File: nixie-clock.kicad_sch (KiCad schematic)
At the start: 80 parts, among them J1 I2C, J2 SWD, J3 ESP-Connector, J4 Power Input, J5 ARGB, Q1 FDS2734, SW1 PTS815, U1 TPS62175DQC, U2 STM32F103CBTx, U3 TC1185, U4 LT3757AEMSE, U5 Dot1, U6 Dot2, U7 USBLC6-2SC6

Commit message: Add PCB and update Schematic
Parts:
- removed C18: 100n, symbol Device:C
- removed D2, D3, D4, D5, D6, D7: APA102, LED_SMD:LED_RGB_5050-6, symbol LED:APA102
- removed R10, R9: 3k9, symbol Device:R
- added C21: 220n 35V, Capacitor_SMD:C_0805_2012Metric_Pad1.18x1.45mm_HandSolder, symbol Device:C
- added H7, H8, H9: MountingHole_Pad, MountingHole:MountingHole_3.2mm_M3_ISO14580, symbol Mechanical:MountingHole
- added TP1: GND, TestPoint:TestPoint_THTPad_D1.5mm_Drill0.7mm, symbol Connector:TestPoint
- added TP2: 3V3, TestPoint:TestPoint_THTPad_D1.5mm_Drill0.7mm, symbol Connector:TestPoint
- added TP3: 5V, TestPoint:TestPoint_THTPad_D1.5mm_Drill0.7mm, symbol Connector:TestPoint
- added TP4: 190V, TestPoint:TestPoint_THTPad_D1.5mm_Drill0.7mm, symbol Connector:TestPoint
- added TP5: TimeSync, TestPoint:TestPoint_THTPad_D1.5mm_Drill0.7mm, symbol Connector:TestPoint
- C1, C3: footprint (none) -> Capacitor_SMD:C_0805_2012Metric_Pad1.18x1.45mm_HandSolder
- C10: renamed from C9; footprint (none) -> Capacitor_SMD:C_0603_1608Metric_Pad1.08x0.95mm_HandSolder
- C11: renamed from C12; footprint (none) -> Capacitor_SMD:C_0603_1608Metric_Pad1.08x0.95mm_HandSolder
- C12: renamed from C11; footprint (none) -> Capacitor_SMD:C_0402_1005Metric_Pad0.74x0.62mm_HandSolder
- C13: renamed from C14; footprint (none) -> Capacitor_SMD:C_0603_1608Metric_Pad1.08x0.95mm_HandSolder
- C14: renamed from C15; footprint (none) -> Capacitor_SMD:C_0805_2012Metric_Pad1.18x1.45mm_HandSolder
- C15: renamed from C10; footprint (none) -> Capacitor_SMD:C_0603_1608Metric_Pad1.08x0.95mm_HandSolder
- C16, C20: footprint (none) -> Capacitor_SMD:C_0603_1608Metric_Pad1.08x0.95mm_HandSolder
- C17: renamed from C13; footprint (none) -> Capacitor_SMD:C_0603_1608Metric_Pad1.08x0.95mm_HandSolder
- C18: renamed from C19; footprint (none) -> Capacitor_SMD:C_0402_1005Metric_Pad0.74x0.62mm_HandSolder
- C19: renamed from C17; footprint (none) -> Capacitor_SMD:C_1206_3216Metric_Pad1.33x1.80mm_HandSolder
- C22: renamed from C21; value 10u -> 10u 16V; footprint (none) -> Capacitor_SMD:C_0805_2012Metric_Pad1.18x1.45mm_HandSolder
- C23: renamed from C22; footprint (none) -> Capacitor_SMD:C_0603_1608Metric_Pad1.08x0.95mm_HandSolder
- C4: renamed from C24; footprint (none) -> Capacitor_SMD:C_0603_1608Metric_Pad1.08x0.95mm_HandSolder
- C6: renamed from C5; footprint Capacitor_SMD:C_0603_1608Metric_Pad1.08x0.95mm_HandSolder -> Capacitor_SMD:C_0805_2012Metric_Pad1.18x1.45mm_HandSolder
- C7: renamed from C6; footprint (none) -> Capacitor_SMD:C_0805_2012Metric_Pad1.18x1.45mm_HandSolder
- C8: renamed from C7; footprint (none) -> Capacitor_SMD:C_0805_2012Metric_Pad1.18x1.45mm_HandSolder
- C9: renamed from C8; footprint (none) -> Capacitor_SMD:C_0603_1608Metric_Pad1.08x0.95mm_HandSolder
- D1: value D -> HS1FFL; footprint (none) -> Diode_SMD:D_SOD-123F
- L2: value 470u -> 470u (NS12555T471MN); footprint (none) -> extraFootprints:Taiyo Yuden NS 12.5mmx12.5mm
- R1: renamed from R60; footprint (none) -> Resistor_SMD:R_0603_1608Metric_Pad0.98x0.95mm_HandSolder
- R10: renamed from R4; footprint (none) -> Resistor_SMD:R_0603_1608Metric_Pad0.98x0.95mm_HandSolder
- R11: renamed from R5; footprint (none) -> Resistor_SMD:R_0603_1608Metric_Pad0.98x0.95mm_HandSolder
- R12: renamed from R6; footprint (none) -> Resistor_SMD:R_0603_1608Metric_Pad0.98x0.95mm_HandSolder
- R13: renamed from R7; footprint (none) -> Resistor_SMD:R_1206_3216Metric_Pad1.30x1.75mm_HandSolder
- R14: renamed from R8; footprint (none) -> Resistor_SMD:R_0603_1608Metric_Pad0.98x0.95mm_HandSolder
- R15: renamed from R65; value R -> 56k; footprint (none) -> Resistor_SMD:R_0603_1608Metric_Pad0.98x0.95mm_HandSolder
- R16: renamed from R66; value R -> 56k; footprint (none) -> Resistor_SMD:R_0603_1608Metric_Pad0.98x0.95mm_HandSolder
- R2: renamed from R59; footprint (none) -> Resistor_SMD:R_0603_1608Metric_Pad0.98x0.95mm_HandSolder
- R3: renamed from R67; footprint (none) -> Resistor_SMD:R_0603_1608Metric_Pad0.98x0.95mm_HandSolder
- R4: renamed from R1; footprint Resistor_SMD:R_0603_1608Metric_Pad1.05x0.95mm_HandSolder -> Resistor_SMD:R_0603_1608Metric_Pad0.98x0.95mm_HandSolder
- R5: renamed from R2; footprint Resistor_SMD:R_0603_1608Metric_Pad1.05x0.95mm_HandSolder -> Resistor_SMD:R_0603_1608Metric_Pad0.98x0.95mm_HandSolder
- R6: renamed from R69; footprint (none) -> Resistor_SMD:R_1206_3216Metric_Pad1.30x1.75mm_HandSolder
- R7: renamed from R70; footprint (none) -> Resistor_SMD:R_0603_1608Metric_Pad0.98x0.95mm_HandSolder
- R8: renamed from R68; footprint (none) -> Resistor_SMD:R_0603_1608Metric_Pad0.98x0.95mm_HandSolder
- R9: renamed from R3; footprint (none) -> Resistor_SMD:R_0603_1608Metric_Pad0.98x0.95mm_HandSolder
- renumbered C23 to C24, C4 to C5, D8 to D2, J4 to J1, J5 to J2, J1 to J3, J2 to J4, J3 to J5, U7 to U2, U2 to U3, U3 to U4, U4 to U5, U5 to U6, U6 to U7
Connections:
- net +24V: now also C21.1
- net +3V3: now also TP2.1
- net +5V: now also TP3.1
- net GND: now also J1.1 (Pin_1), R15.2, R16.2, C21.2, TP1.1; no longer J1.2 (Pin_2), U6.7 (K), U7.7 (K)
- net TimeSync: now also TP5.1
- net Vdrive: now also TP4.1
- net high-side-switch6/Dot: now also U6.1 (A), U7.1 (A); no longer R15.1, R16.1
- net ledClock: now also U2.1 (I/O1); no longer U2.6 (I/O1)
- net ledData: now also U2.6 (I/O1); no longer U2.4 (I/O2)
- net at J2.3 (Pin_3): now also U2.3 (I/O2)
- net at J2.2 (Pin_2): now also U2.4 (I/O2)
- net at F1.1: now also J1.2 (Pin_2); no longer J1.1 (Pin_1)
- new net: R15.1, U6.2 (K)
- new net: R16.1, U7.2 (K)
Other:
- sheet low-side-switch10 renamed low-side-switch-dp-left
- removed sheet low-side-switch11
- added sheet low-side-switch-dp-right (low-side-switch-dp.kicad_sch)
- sheet low-side-switch-dp-left: file low-side-switch.kicad_sch -> low-side-switch-dp.kicad_sch
- note added: "LED mounting"
- note added: "PCB mounting"
- note added: "Reduce Hot Loop Area to minimize EMI: Linear Technology AN139-1 Texas Instruments SNVA803"
- note added: "connector for addressable LEDs"
- note added: "test points"
- note removed: "addressable LEDs"
- note removed: "mounting"
- moved on the sheet: C15, C16, C17, C18, C19, C20, C22, C23, C24, C4, D1, D2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

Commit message: Add dimming option
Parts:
- added C25: 100n, Capacitor_SMD:C_0603_1608Metric_Pad1.08x0.95mm_HandSolder, symbol Device:C
- added C26: 1u, Capacitor_SMD:C_0805_2012Metric_Pad1.18x1.45mm_HandSolder, symbol Device:C
- added R71: 10k, Resistor_SMD:R_0603_1608Metric_Pad0.98x0.95mm_HandSolder, symbol Device:R
- added U8: SN74HCS541, extraFootprints:VSSOP-20_5.1x3mm_P0.5mm, symbol extraSymbols:SN74HCS541
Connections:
- net +3V3: now also C25.2, C26.2, R71.1, U8.20 (V_{CC})
- net Enable.Dots: now also U8.8 (A7)
- net Enable.Tube0: now also U8.2 (A1)
- net Enable.Tube1: now also U8.3 (A2)
- net Enable.Tube2: now also U8.4 (A3)
- net Enable.Tube3: now also U8.5 (A4)
- net Enable.Tube4: now also U8.6 (A5)
- net Enable.Tube5: now also U8.7 (A6)
- net GND: now also C25.1, C26.1, U8.10 (GND), U8.9 (A8)
- net ~{PWM}: now reaches U3.19 (PB1)
- net ~{PWM}: now also R71.2, U8.1 (~{OE1}), U8.19 (~{OE2})
- new net high-side-switch/Enable: U8.18 (Y1)
- new net high-side-switch1/Enable: U8.17 (Y2)
- new net high-side-switch2/Enable: U8.16 (Y3)
- new net high-side-switch3/Enable: U8.15 (Y4)
- new net high-side-switch4/Enable: U8.14 (Y5)
- new net high-side-switch5/Enable: U8.13 (Y6)
- new net high-side-switch6/Enable: U8.12 (Y7)
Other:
- note added: "IC buffer for PWM dimming"
- moved on the sheet: C1, C10, C11, C12, C13, C14, C15, C16, C17, C18, C19, C2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

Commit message: Some finish workings
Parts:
- C23: footprint Capacitor_SMD:C_0603_1608Metric_Pad1.08x0.95mm_HandSolder -> Capacitor_SMD:C_0805_2012Metric_Pad1.18x1.45mm_HandSolder
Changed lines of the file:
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@@
 			)
 		)
-		(property "Footprint" "Capacitor_SMD:C_0603_1608Metric_Pad1.08x0.95mm_HandSolder"
+		(property "Footprint" "Capacitor_SMD:C_0805_2012Metric_Pad1.18x1.45mm_HandSolder"
 			(at 343.8652 217.17 0)
 			(effects

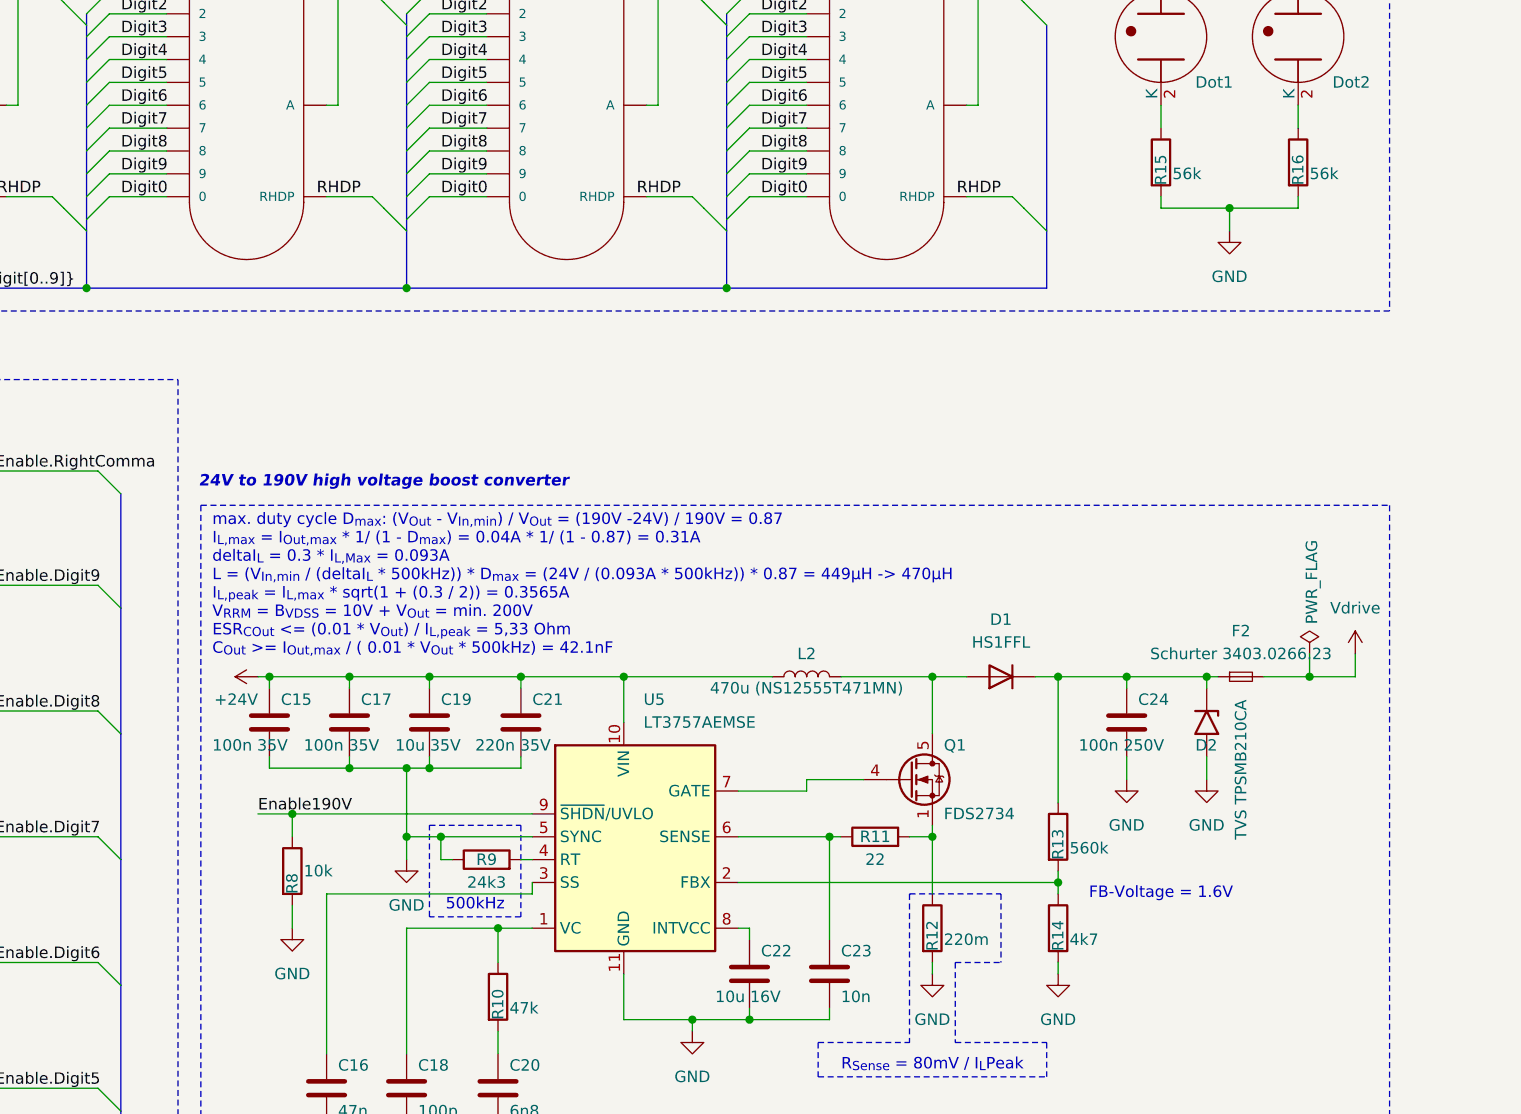
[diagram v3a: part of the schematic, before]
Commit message: Update values to soldered ones
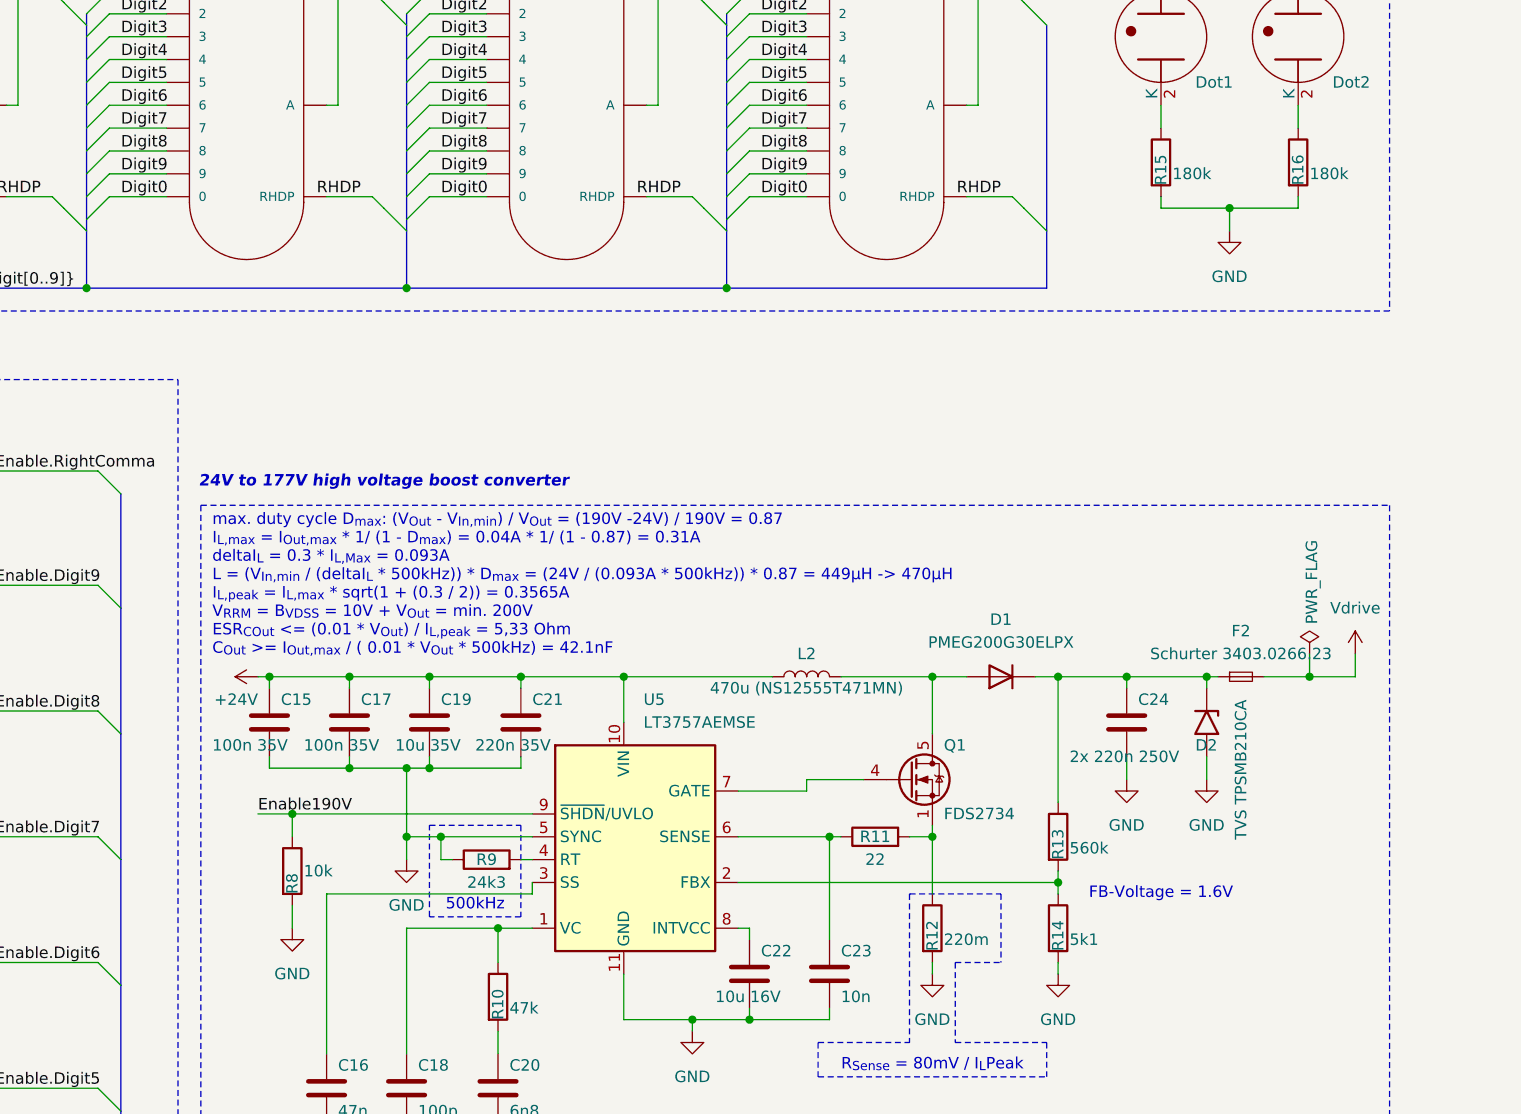
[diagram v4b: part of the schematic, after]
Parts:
- C24: value 100n 250V -> 2x 220n 250V
- D1: value HS1FFL -> PMEG200G30ELPX
- R14: value 4k7 -> 5k1
- R15, R16: value 56k -> 180k
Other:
- note added: "24V to 177V high voltage boost converter"
- note removed: "24V to 190V high voltage boost converter"
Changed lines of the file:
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@@
 		)
 	)
-	(text "24V to 190V high voltage boost converter"
+	(text "24V to 177V high voltage boost converter"
 		(exclude_from_sim no)
 		(at 293.37 158.75 0)
@@
 			)
 		)
-		(property "Value" "56k"
+		(property "Value" "180k"
 			(at 396.24 124.46 0)
 			(effects
@@
 			)
 		)
-		(property "Value" "56k"
+		(property "Value" "180k"
 			(at 381 124.46 0)
 			(effects
@@
 			)
 		)
-		(property "Value" "100n 250V"
-			(at 370.586 187.96 0)
+		(property "Value" "2x 220n 250V"
+			(at 369.57 189.23 0)
 			(effects
 				(font
@@
 			)
 		)
-		(property "Value" "HS1FFL"
+		(property "Value" "PMEG200G30ELPX"
 			(at 361.95 176.53 0)
 			(effects
@@
 			)
 		)
-		(property "Datasheet" "https://www.taiwansemi.com/assets/datasheet/pdf.php?pn=HS1FFL"
+		(property "Datasheet" "https://www.mouser.de/datasheet/2/916/PMEG200G30ELP-2634407.pdf"
 			(at 361.95 180.34 0)
 			(effects
@@
 			)
 		)
-		(property "Value" "4k7"
+		(property "Value" "5k1"
 			(at 369.57 209.55 0)
 			(effects

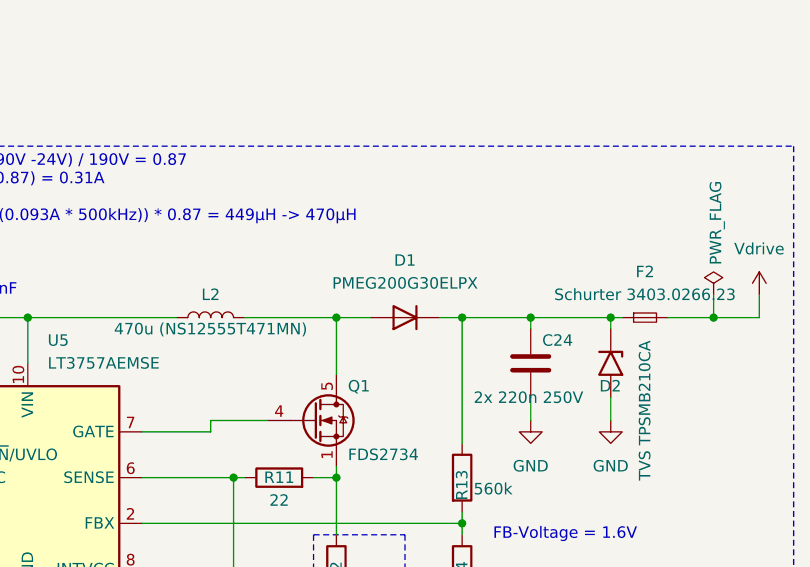
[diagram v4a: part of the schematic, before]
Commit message: Change diode in boost converter circuit
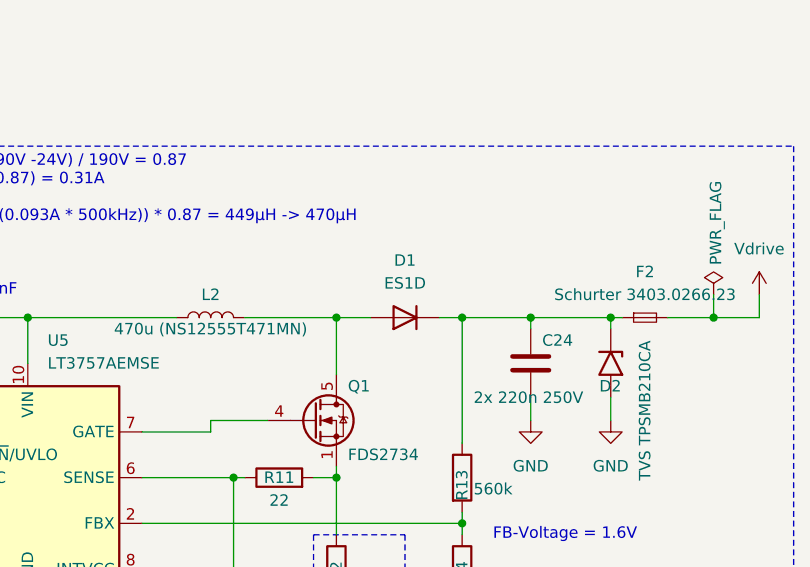
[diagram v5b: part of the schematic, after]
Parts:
- D1: value PMEG200G30ELPX -> ES1D
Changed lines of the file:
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@@
 			)
 		)
-		(property "Value" "PMEG200G30ELPX"
+		(property "Value" "ES1D"
 			(at 361.95 176.53 0)
 			(effects
@@
 			)
 		)
-		(property "Datasheet" "https://www.mouser.de/datasheet/2/916/PMEG200G30ELP-2634407.pdf"
+		(property "Datasheet" "https://www.onsemi.com/pdf/datasheet/es1d-d.pdf"
 			(at 361.95 180.34 0)
 			(effects

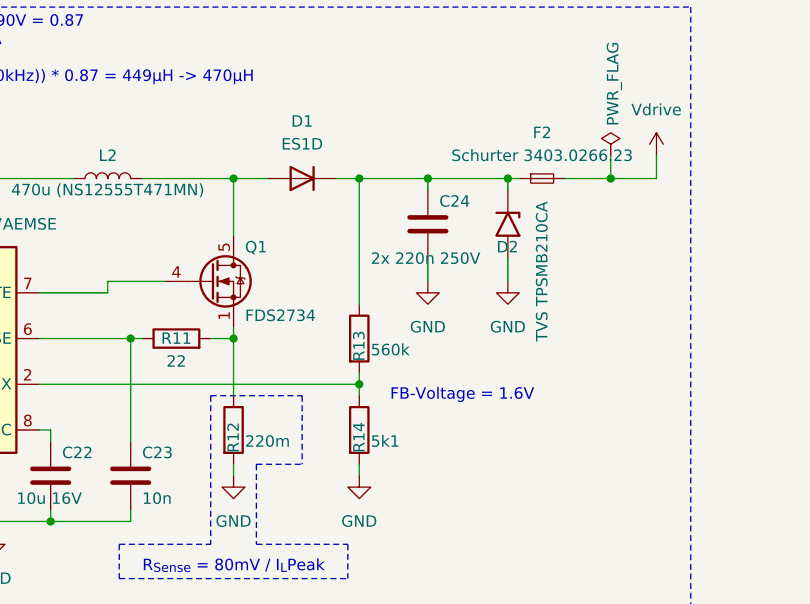
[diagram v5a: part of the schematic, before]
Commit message: Add know issues to ReadMe, change some values according to simulation
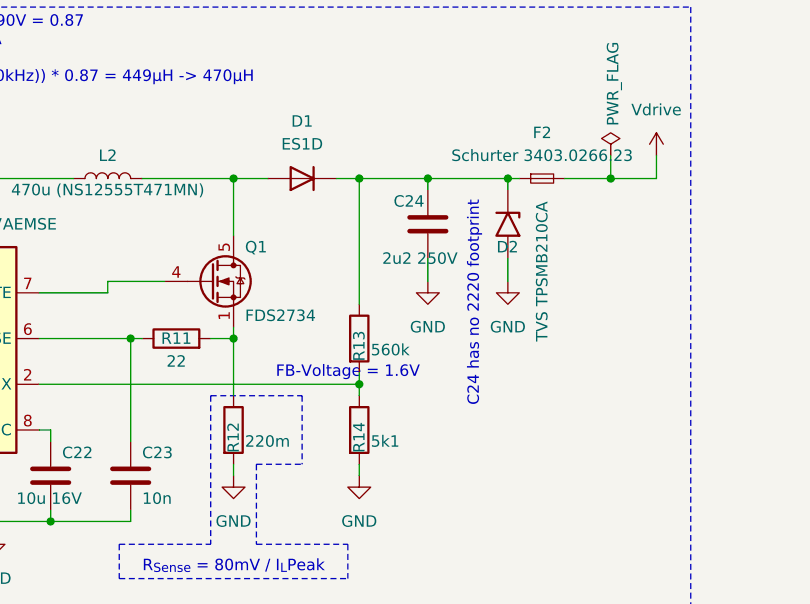
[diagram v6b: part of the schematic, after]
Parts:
- C24: value 2x 220n 250V -> 2u2 250V
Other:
- note added: "C24 has no 2220 footprint"
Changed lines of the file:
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@@
 	(text "FB-Voltage = 1.6V"
 		(exclude_from_sim no)
-		(at 379.73 204.47 0)
+		(at 367.03 201.93 0)
 		(effects
 			(font
@@
 		)
 	)
+	(text "C24 has no 2220 footprint"
+		(exclude_from_sim no)
+		(at 381 194.31 90)
+		(effects
+			(font
+				(size 1.27 1.27)
+			)
+		)
+	)
 	(text "pulse voltage: 190V\npulse current: max. 13mA\npulse current (commatas): max. 5mA"
 		(exclude_from_sim no)
@@
 		(dnp no)
 		(property "Reference" "C24"
-			(at 377.19 182.88 0)
+			(at 372.11 182.88 0)
 			(effects
 				(font
@@
 			)
 		)
-		(property "Value" "2x 220n 250V"
-			(at 369.57 189.23 0)
+		(property "Value" "2u2 250V"
+			(at 370.84 189.23 0)
 			(effects
 				(font
